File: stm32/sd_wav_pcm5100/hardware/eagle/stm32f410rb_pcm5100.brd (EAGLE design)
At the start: 46.1 x 58.2 mm, 33 parts, among them IC1 STM32F410, U5 PCM5100

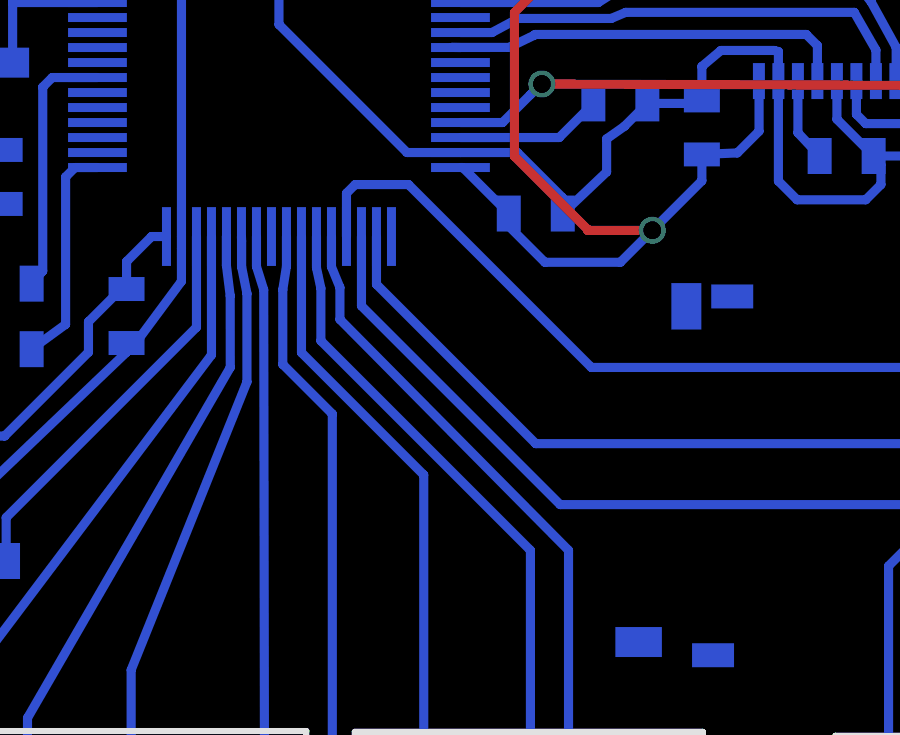
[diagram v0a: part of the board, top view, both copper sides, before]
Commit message: [stm32/sd_wav_pcm5100] SPI DI/DO lines were inversed
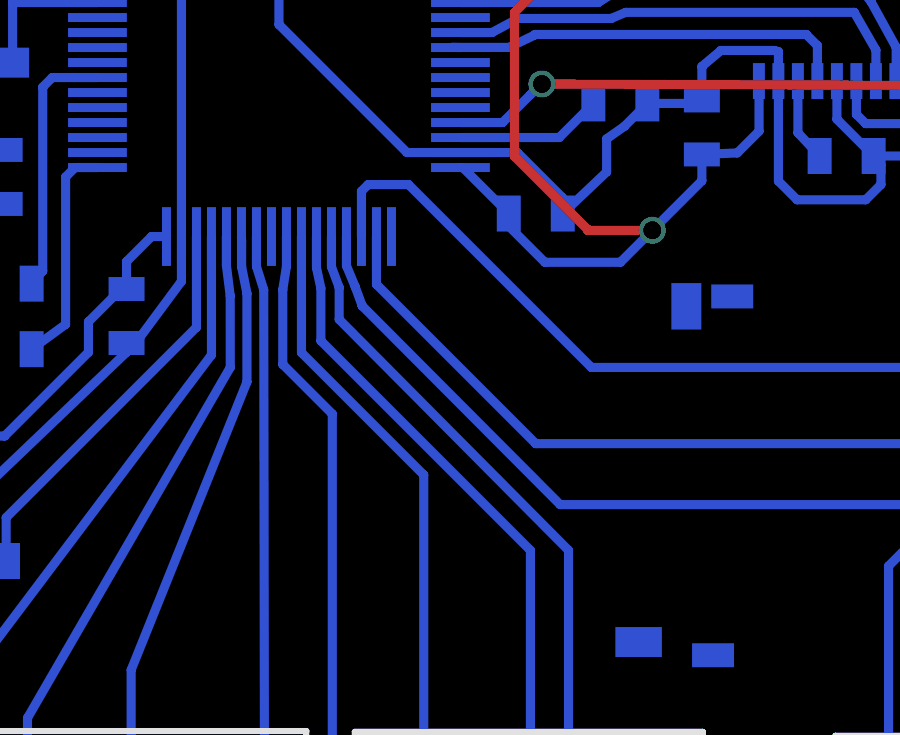
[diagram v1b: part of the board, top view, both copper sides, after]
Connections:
- net SD_DI: now also IC1.36; no longer IC1.35
- net SD_DO: now also IC1.35; no longer IC1.36
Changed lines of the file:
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@@
 <signal name="SD_DI">
 <contactref element="MMC1" pad="CMD/RESP"/>
-<contactref element="IC1" pad="35"/>
-<wire x1="19.514" y1="25.954" x2="19.514" y2="23.6406" width="0.3048" layer="16"/>
 <wire x1="26.1366" y1="17.018" x2="39.5935" y2="17.018" width="0.3048" layer="16"/>
 <wire x1="39.5935" y1="17.018" x2="39.673" y2="17.0975" width="0.3048" layer="16"/>
-<wire x1="26.1366" y1="17.018" x2="19.514" y2="23.6406" width="0.3048" layer="16"/>
+<wire x1="26.1366" y1="17.018" x2="19.5394" y2="23.6406" width="0.3048" layer="16"/>
+<contactref element="IC1" pad="36"/>
+<wire x1="19.014" y1="25.954" x2="19.014" y2="24.9788" width="0.3048" layer="16"/>
+<wire x1="19.014" y1="24.9788" x2="19.304" y2="24.2824" width="0.3048" layer="16"/>
+<wire x1="19.304" y1="24.2824" x2="19.5326" y2="23.6592" width="0.3048" layer="16"/>
+<wire x1="19.5326" y1="23.6592" x2="19.5394" y2="23.6406" width="0.3048" layer="16"/>
 </signal>
 <signal name="SD_DO">
 <contactref element="MMC1" pad="DAT0"/>
-<contactref element="IC1" pad="36"/>
-<wire x1="19.014" y1="25.954" x2="19.014" y2="27.396" width="0.3048" layer="16"/>
-<wire x1="19.014" y1="27.396" x2="19.304" y2="27.686" width="0.3048" layer="16"/>
-<wire x1="19.304" y1="27.686" x2="21.082" y2="27.686" width="0.3048" layer="16"/>
 <wire x1="21.082" y1="27.686" x2="27.178" y2="21.59" width="0.3048" layer="16"/>
 <wire x1="27.178" y1="21.59" x2="39.5805" y2="21.59" width="0.3048" layer="16"/>
 <wire x1="39.5805" y1="21.59" x2="39.673" y2="21.4975" width="0.3048" layer="16"/>
+<contactref element="IC1" pad="35"/>
+<wire x1="21.082" y1="27.686" x2="19.7358" y2="27.686" width="0.3048" layer="16"/>
+<wire x1="19.7358" y1="27.686" x2="19.514" y2="27.4642" width="0.3048" layer="16"/>
+<wire x1="19.514" y1="25.954" x2="19.514" y2="27.4642" width="0.3048" layer="16"/>
 </signal>
 <signal name="SD_SCLK">
@@
 <wire x1="26.416" y1="8.27" x2="28.59" y2="6.0452" width="0.3048" layer="16"/>
 <wire x1="18.514" y1="25.954" x2="18.514" y2="24.9454" width="0.3048" layer="16"/>
-<wire x1="18.514" y1="24.9454" x2="18.796" y2="24.257" width="0.3048" layer="16"/>
-<wire x1="18.796" y1="24.257" x2="18.796" y2="23.1902" width="0.3048" layer="16"/>
-<wire x1="18.796" y1="23.1902" x2="26.416" y2="15.494" width="0.3048" layer="16"/>
+<wire x1="18.514" y1="24.9454" x2="18.7706" y2="24.257" width="0.3048" layer="16"/>
+<wire x1="18.7706" y1="24.257" x2="18.7706" y2="23.1902" width="0.3048" layer="16"/>
+<wire x1="18.7706" y1="23.1902" x2="26.416" y2="15.494" width="0.3048" layer="16"/>
 </signal>
 <signal name="N$22">
